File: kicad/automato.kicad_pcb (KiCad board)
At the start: 2 copper layers, 106 x 64 mm, 99 parts, among them J1 USB_C_Receptacle, J2 LiPo, J3 Conn_01x07_Male, J4 Screw_Terminal_01x20, J5 USB_C_Receptacle, J6 Conn_Coaxial, J8 Micro_SD_Card_Det, M1 eink-module, Q1 Q_NPN_BCE, Q2 Q_NPN_BCE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

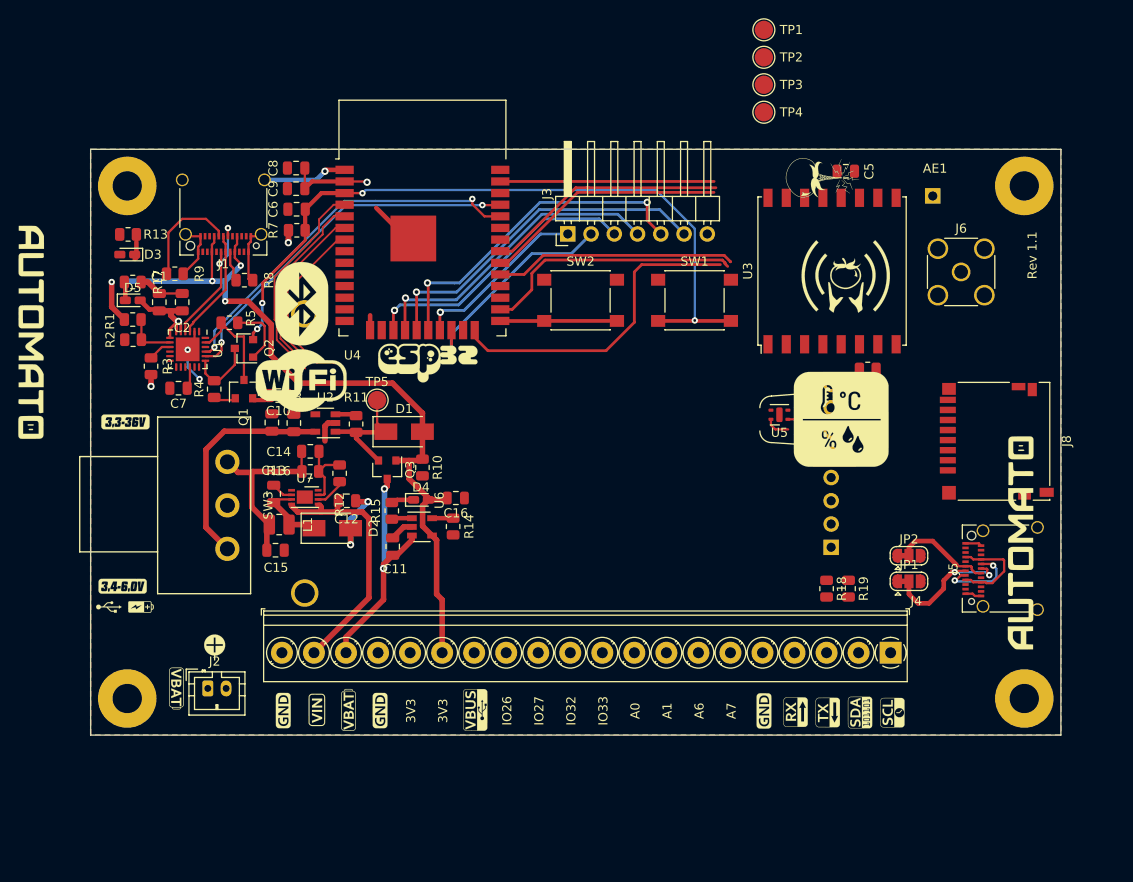
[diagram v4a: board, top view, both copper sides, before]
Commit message: keep routing, add qwiic connectors, change layout to optimize for density and rf
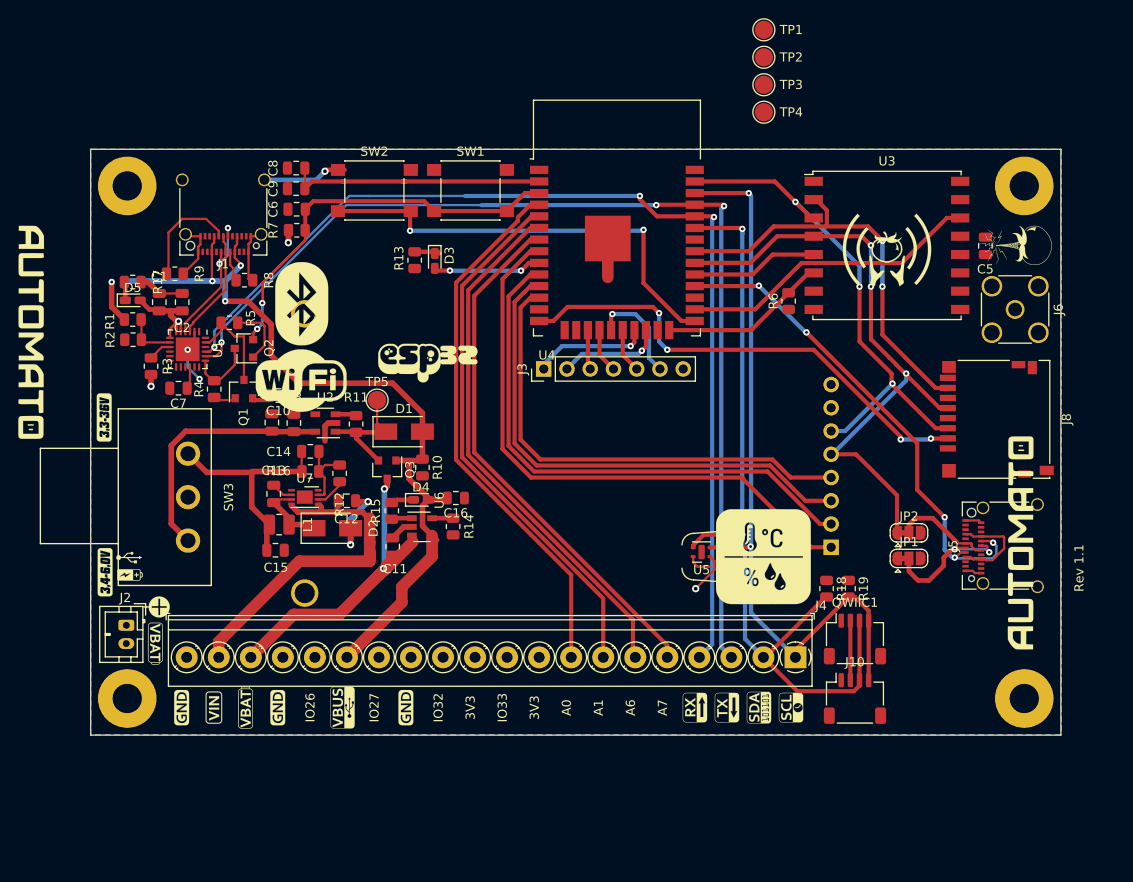
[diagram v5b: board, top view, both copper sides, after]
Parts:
- removed AE1: Antenna, Connector_PinHeader_2.54mm:PinHeader_1x01_P2.54mm_Vertical
- added J10: QWIIC 0, Connector_JST:JST_SH_SM04B-SRSS-TB_1x04-1MP_P1.00mm_Horizontal, F.Cu at (163.5, 117.0)
- added QWIIC1: QWIIC 1, Connector_JST:JST_SH_SM04B-SRSS-TB_1x04-1MP_P1.00mm_Horizontal, F.Cu at (163.5, 110.5)
- J3: footprint Connector_PinHeader_2.54mm:PinHeader_1x07_P2.54mm_Horizontal -> Connector_PinHeader_2.54mm:PinHeader_1x07_P2.54mm_Vertical
- moved G*** 114.1 mm to (246.9, 90.0)
- moved G*** 39.1 mm to (114.5, 118.0)
- moved D3 33.6 mm to (117.6, 69.2), turned to 270 degrees
- moved R13 31.4 mm to (115.4, 69.1), turned to 270 degrees
- moved SW1 27.3 mm to (121.5, 61.5)
- moved SW2 25.5 mm to (111.0, 61.5)
- moved G*** 22.3 mm to (181.0, 67.5), turned to 90 degrees
- moved U4 21.2 mm to (137.5, 67.5)
- moved C5 17.3 mm to (177.8, 67.5), turned to 270 degrees
- moved G*** 17.2 mm to (153.5, 101.5)
- moved U5 17.2 mm to (146.8, 101.0)
- moved J3 15.0 mm to (129.5, 81.0)
- moved G*** 14.5 mm to (107.5, 118.0)
- moved R6 11.4 mm to (156.2, 73.6), turned to 90 degrees
- moved J2 11.3 mm to (83.9, 109.0), turned to 270 degrees
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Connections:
- J5 pad A4: VBUS -> 3V3
- J5 pad A9: VBUS -> 3V3
- J5 pad B4: VBUS -> 3V3
- J5 pad B9: VBUS -> 3V3
- J8 pad 2: SD_CS -> CS_SD
- U4 pad 10: BUSY_EINK -> RST_EINK
- U4 pad 11: RST_EINK -> DC_EINK
- U4 pad 12: DC_EINK -> CS_EINK
- U4 pad 8: CS_EINK -> BUSY_EINK
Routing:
- net I2C_SDA: track 0.00 -> 88.2 mm, vias 0 -> 2
- net I2C_SCL: track 0.00 -> 82.6 mm, vias 0 -> 2
- net TX: track 40.6 -> 115.0 mm, vias 2 -> 3
- net RX: track 41.6 -> 114.1 mm, vias 2 -> 3
- net BUSY_EINK: track 0.00 -> 64.2 mm
- net RST_EINK: track 0.00 -> 59.5 mm
- net DC_EINK: track 0.00 -> 56.0 mm
- net CS_SD: track 0.00 -> 53.3 mm, vias 0 -> 4
- net CS_EINK: track 0.00 -> 52.5 mm
- net CS_RELAY: track 9.00 -> 54.8 mm, vias 2 -> 5
- net SPI_CLK: track 26.5 -> 68.3 mm, vias 0 -> 3
- net 3V3: track 29.2 -> 68.9 mm, vias 5 -> 4
- net A6: track 19.0 -> 58.2 mm
- net A7: track 19.8 -> 57.9 mm
- net A1: track 20.9 -> 58.5 mm
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
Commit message: route gpoi's
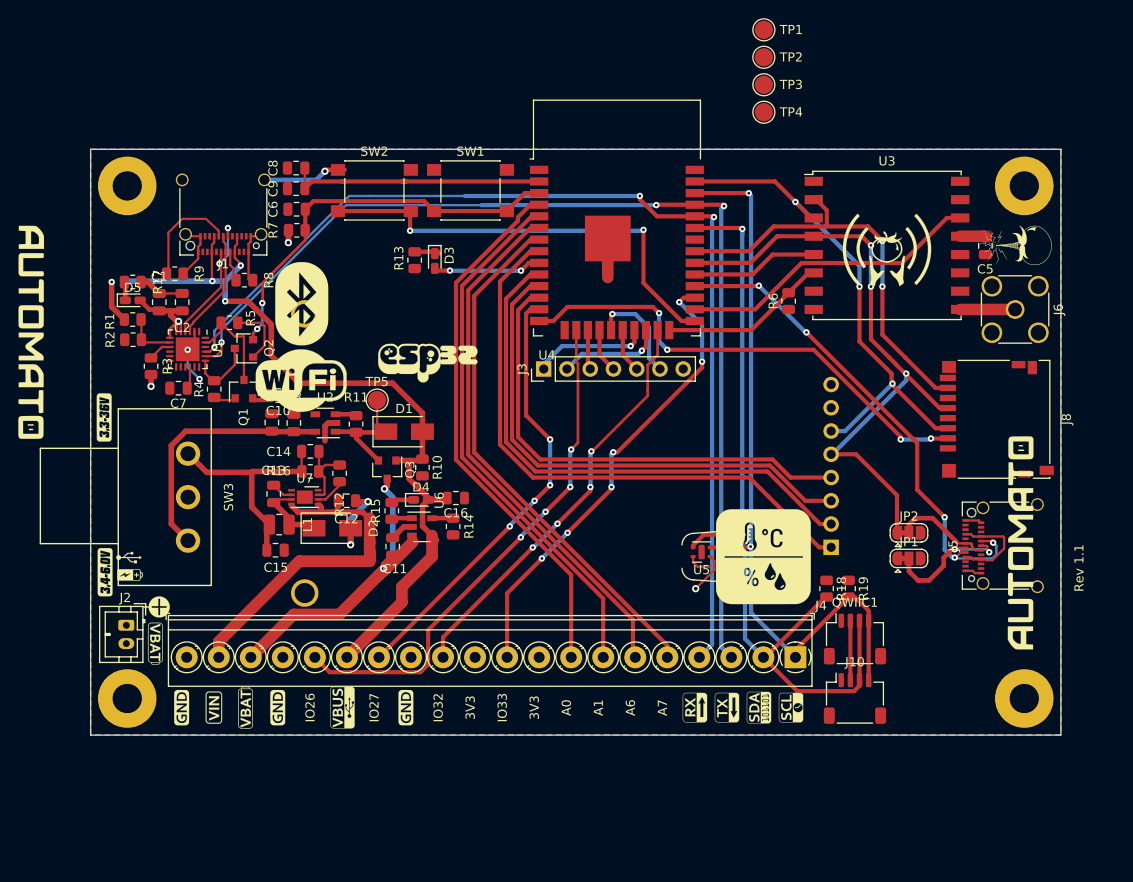
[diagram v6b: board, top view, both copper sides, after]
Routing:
- net IO13: track 0.00 -> 56.8 mm, vias 0 -> 4
- net IO16: track 0.00 -> 50.8 mm, vias 0 -> 6
- net IO14: track 0.00 -> 48.0 mm, vias 0 -> 4
- net IO15: track 0.00 -> 45.8 mm, vias 0 -> 4
- net Net-(J6-Pad1): track 0.00 -> 6.00 mm
- net 3V3: track 68.9 -> 71.7 mm
- net VBAT: track 38.1 -> 38.8 mm

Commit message: add jst, re-route
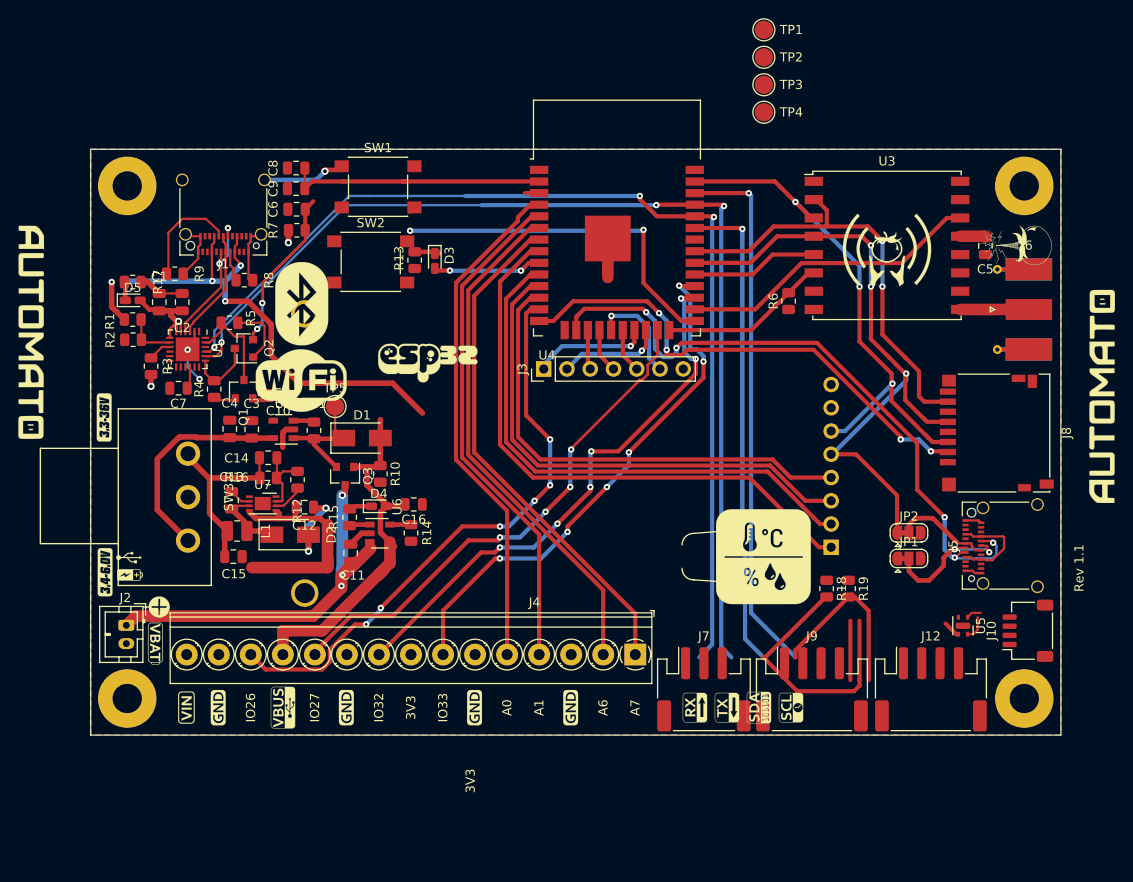
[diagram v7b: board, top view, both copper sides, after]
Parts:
- removed the G*** at (97.0, 118.0)
- removed QWIIC1: QWIIC 1, Connector_JST:JST_SH_SM04B-SRSS-TB_1x04-1MP_P1.00mm_Horizontal
- added G***: LOGO, logo:GND, F.Cu at (132.5, 118.0)
- added J12: STEMMA 0, Connector_JST:JST_PH_S4B-PH-SM4-TB_1x04-1MP_P2.00mm_Horizontal, F.Cu at (171.8, 116.0)
- added J7: 1-WIRE, Connector_JST:JST_PH_S3B-PH-SM4-TB_1x03-1MP_P2.00mm_Horizontal, F.Cu at (147.0, 116.0)
- added J9: UART2, Connector_JST:JST_PH_S4B-PH-SM4-TB_1x04-1MP_P2.00mm_Horizontal, F.Cu at (158.8, 116.0)
- J4: value Screw_Terminal_01x20 -> Screw_Terminal_01x15; footprint automato-sensor:TerminalBlock_Phoenix_PT-1,5-20-3.5-H_1x20_P3.50mm_Horizontal -> TerminalBlock_Phoenix:TerminalBlock_Phoenix_PT-1,5-15-3.5-H_1x15_P3.50mm_Horizontal
- J6: footprint Connector_Coaxial:SMA_Wurth_60312002114503_Vertical -> Connector_Coaxial:SMA_Molex_73251-1153_EdgeMount_Horizontal
- moved U5 29.7 mm to (175.3, 109.0), turned to 270 degrees
- moved J10 20.3 mm to (182.4, 109.6), turned to 90 degrees
- moved G*** 18.3 mm to (190.5, 84.0)
- moved J4 17.5 mm to (139.5, 112.2)
- moved SW1 10.1 mm to (111.4, 61.1)
- moved SW2 7.81 mm to (110.6, 69.3)
- moved G*** 7.50 mm to (122.0, 118.0)
- moved G*** 7.50 mm to (108.0, 118.0)
- moved G*** 6.50 mm to (101.0, 118.0)
- moved C15 4.65 mm to (95.6, 101.5)
- moved C16 4.65 mm to (115.3, 95.8)
- moved D4 4.65 mm to (111.5, 96.0)
- moved Q3 4.65 mm to (107.8, 92.7)
- moved R15 4.65 mm to (108.3, 97.2)
- moved U6 4.65 mm to (111.6, 99.0)
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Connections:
- J4 pad 1: I2C_SCL -> A7
- J4 pad 10: IO16 -> GND
- J4 pad 11: 3V3 -> IO14
- J4 pad 12: IO15 -> VBUS
- J4 pad 13: GND -> IO13
- J4 pad 14: IO14 -> GND
- J4 pad 15: VBUS -> VIN
- J4 pad 2: I2C_SDA -> A6
- J4 pad 3: TX -> GND
- J4 pad 4: RX -> A1
- J4 pad 5: A7 -> A0
- J4 pad 6: A6 -> GND
- J4 pad 7: A1 -> IO16
- J4 pad 8: A0 -> 3V3
- J4 pad 9: 3V3 -> IO15
- JP1 pad 3: U2_RXD -> IO15
- JP2 pad 3: U2_TXD -> IO16
- U4 pad 13: IO14 -> IO13
- U4 pad 16: IO13 -> CS_RELAY
- U4 pad 23: IO15 -> IO14
- U4 pad 27: IO16 -> IO15
- U4 pad 28: CS_RELAY -> IO16
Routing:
- net EN: track 44.4 -> 20.1 mm
- net CS_RELAY: track 54.8 -> 71.8 mm
- net IO15: track 45.8 -> 60.6 mm, vias 4 -> 6
- net VIN: track 38.7 -> 25.1 mm
- net IO0: track 50.9 -> 40.7 mm
- net VBAT: track 38.8 -> 48.2 mm, vias 2 -> 3
- net IO14: track 48.0 -> 57.0 mm
- net IO16: track 50.8 -> 58.3 mm
- net IO13: track 56.8 -> 64.1 mm, vias 4 -> 6
- net I2C_SDA: track 88.2 -> 81.2 mm, vias 2 -> 1
- net I2C_SCL: track 82.6 -> 78.1 mm, vias 2 -> 1
- net Net-(C14-Pad2): track 25.0 -> 20.6 mm
- net Net-(C3-Pad1): track 27.5 -> 23.9 mm
- net VBUS: track 95.4 -> 98.6 mm
- net A1: track 58.5 -> 55.3 mm
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
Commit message: finish JST route
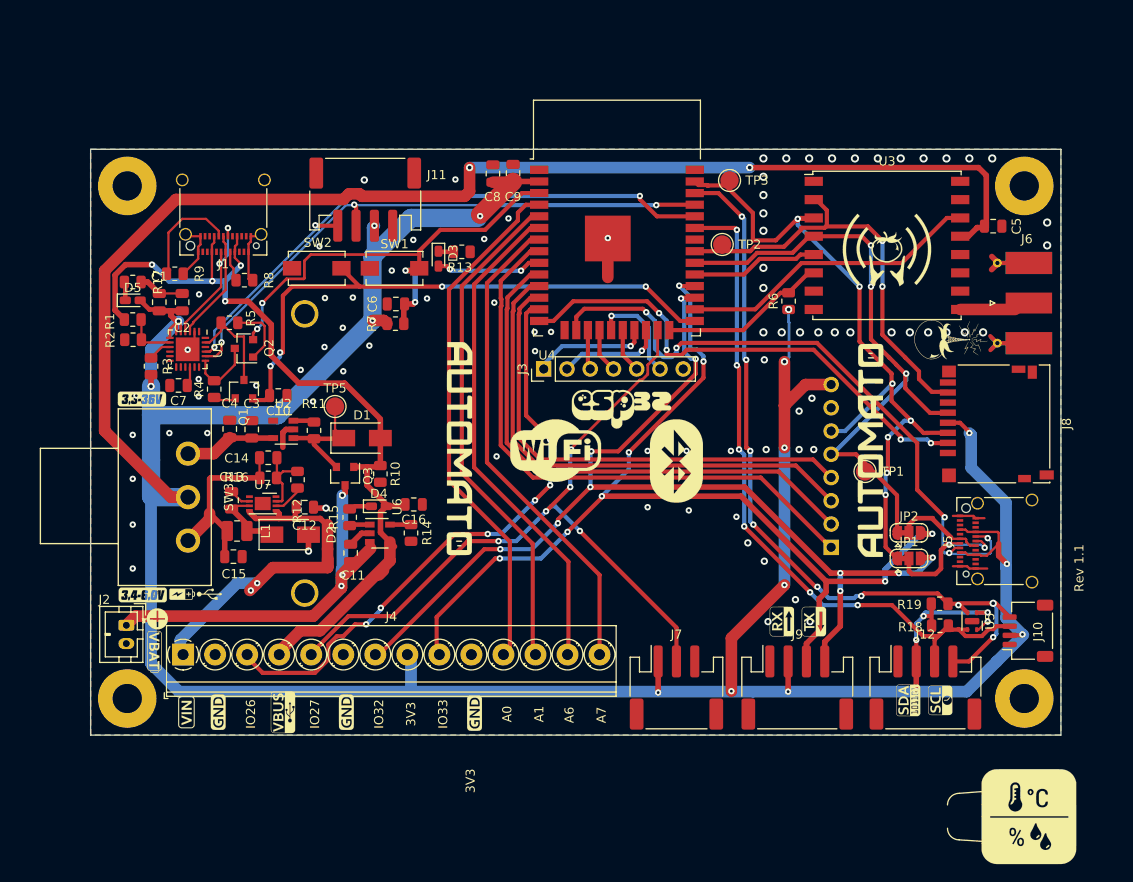
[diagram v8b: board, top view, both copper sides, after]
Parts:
- removed the G*** at (132.5, 118.0)
- removed the G*** at (122.0, 118.0)
- removed TP4: TestPoint, TestPoint:TestPoint_Pad_D2.0mm
- added G***: LOGO, logo:GND, F.Cu at (122.0, 118.6)
- added J11: UART2, Connector_JST:JST_PH_S4B-PH-SM4-TB_1x04-1MP_P2.00mm_Horizontal, F.Cu at (110.0, 62.5)
- J4: value Screw_Terminal_01x15 -> Screw_Terminal_01x14; footprint TerminalBlock_Phoenix:TerminalBlock_Phoenix_PT-1,5-15-3.5-H_1x15_P3.50mm_Horizontal -> TerminalBlock_Phoenix:TerminalBlock_Phoenix_PT-1,5-14-3.5-H_1x14_P3.50mm_Horizontal
- SW1, SW2: footprint Button_Switch_SMD:SW_Push_1P1T_NO_6x6mm_H9.5mm -> Button_Switch_SMD:SW_SPST_EVQPE1
- moved TP1 49.5 mm to (164.6, 92.2)
- moved J4 49.4 mm to (90.1, 112.2), turned to 0 degrees
- moved G*** 48.5 mm to (120.3, 89.7)
- moved G*** 44.4 mm to (144.0, 91.0)
- moved G*** 40.6 mm to (182.5, 129.9)
- moved G*** 28.8 mm to (130.8, 89.9)
- moved G*** 26.0 mm to (165.2, 89.9)
- moved C9 23.8 mm to (126.2, 59.6), turned to 270 degrees
- moved G*** 21.8 mm to (138.0, 85.0)
- moved C8 21.5 mm to (124.0, 59.6), turned to 90 degrees
- moved TP2 21.0 mm to (149.0, 67.4)
- moved G*** 16.3 mm to (172.8, 117.2)
- moved G*** 16.3 mm to (169.3, 117.2)
- moved C6 15.0 mm to (113.3, 73.9)
- moved R7 14.8 mm to (113.3, 76.0)
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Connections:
- C1 pad 1: 3V3 -> +3V3
- C2 pad 1: 3V3 -> +3V3
- C5 pad 1: 3V3 -> +3V3
- C8 pad 1: 3V3 -> +3V3
- C9 pad 2: 3V3 -> +3V3
- D5 pad 2: 3V3 -> +3V3
- J10 pad 2: 3V3 -> +3V3
- J12 pad 2: 3V3 -> +3V3
- J4 pad 1: A7 -> VIN
- J4 pad 11: IO14 -> A0
- J4 pad 12: VBUS -> A1
- J4 pad 13: IO13 -> A6
- J4 pad 14: GND -> A7
- J4 pad 2: A6 -> GND
- J4 pad 3: GND -> IO13
- J4 pad 4: A1 -> VBUS
- J4 pad 5: A0 -> IO14
- J4 pad 7: IO16 -> IO15
- J4 pad 8: 3V3 -> +3V3
- J4 pad 9: IO15 -> IO16
- J5 pad A4: 3V3 -> +3V3
- J5 pad A9: 3V3 -> +3V3
- J5 pad B4: 3V3 -> +3V3
- J5 pad B9: 3V3 -> +3V3
- J7 pad 1: 3V3 -> +3V3
- J8 pad 4: 3v3 -> +3V3
- J9 pad 2: 3V3 -> +3V3
- M1 pad 8: 3V3 -> +3V3
- R18 pad 1: 3V3 -> +3V3
- R19 pad 1: 3V3 -> +3V3
- R3 pad 1: 3V3 -> +3V3
- R6 pad 1: 3V3 -> +3V3
- R7 pad 1: 3V3 -> +3V3
- SW3 pad 1: Net-(C14-Pad2) -> Net-(C3-Pad1)
- SW3 pad 2: 3V3 -> +3V3
- SW3 pad 3: Net-(C3-Pad1) -> Net-(C14-Pad2)
- U1 pad 5: 3V3 -> +3V3
- U1 pad 6: 3V3 -> +3V3
- U1 pad 7: 3V3 -> +3V3
- U3 pad 13: 3V3 -> +3V3
- U4 pad 2: 3V3 -> +3V3
- U5 pad 1: 3V3 -> +3V3
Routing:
- net +3V3: track 0.00 -> 488.2 mm, vias 0 -> 21
- net 3V3: track 68.8 -> 0.00 mm, vias 3 -> 0
- net IO16: track 58.3 -> 112.7 mm, vias 6 -> 8
- net IO15: track 60.6 -> 114.5 mm, vias 6 -> 10
- net TX: track 115.0 -> 64.4 mm
- net RX: track 114.1 -> 66.0 mm
- net EN: track 20.1 -> 52.0 mm, vias 2 -> 4
- net IO14: track 57.0 -> 80.7 mm, vias 4 -> 5
- net IO0: track 40.7 -> 63.5 mm, vias 2 -> 4
- net SPI_MOSI: track 58.3 -> 79.1 mm, vias 3 -> 7
- net VIN: track 25.1 -> 39.0 mm, vias 0 -> 2
- net Net-(C3-Pad1): track 23.9 -> 9.98 mm
- net I2C_SCL: track 78.1 -> 84.0 mm, vias 1 -> 9
- net I2C_SDA: track 81.2 -> 77.6 mm, vias 1 -> 6
- net A7: track 56.5 -> 53.3 mm
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- added copper zone on B.Cu, net GND
- removed copper zone on B.Cu, net 3V3
